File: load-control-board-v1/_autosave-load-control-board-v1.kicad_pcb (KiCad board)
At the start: 4 copper layers, 100 x 80 mm, 94 parts, among them CN1 3511232BMRS0BNA2, CN2 BTC22M4NBB4SCM, CN3 BTC22M4NBB4SCM, Q1 AO3400A, Q2 AO3400A, Q3 IRFP7530PBF, U1 LM317_SOT-223, U10 OPA188xxDBV, U11 OPA188xxDBV, U12 INA186A1IDCKR, U2 74AHC1G04, U22 TL081HIDBVR, U3 LM317_SOT-223, U5 REF5025AD, U6 SN74LVC1G123DCUR_C352969, U7 ALERT_COMP_OUT, U8 OPA188xxDBV

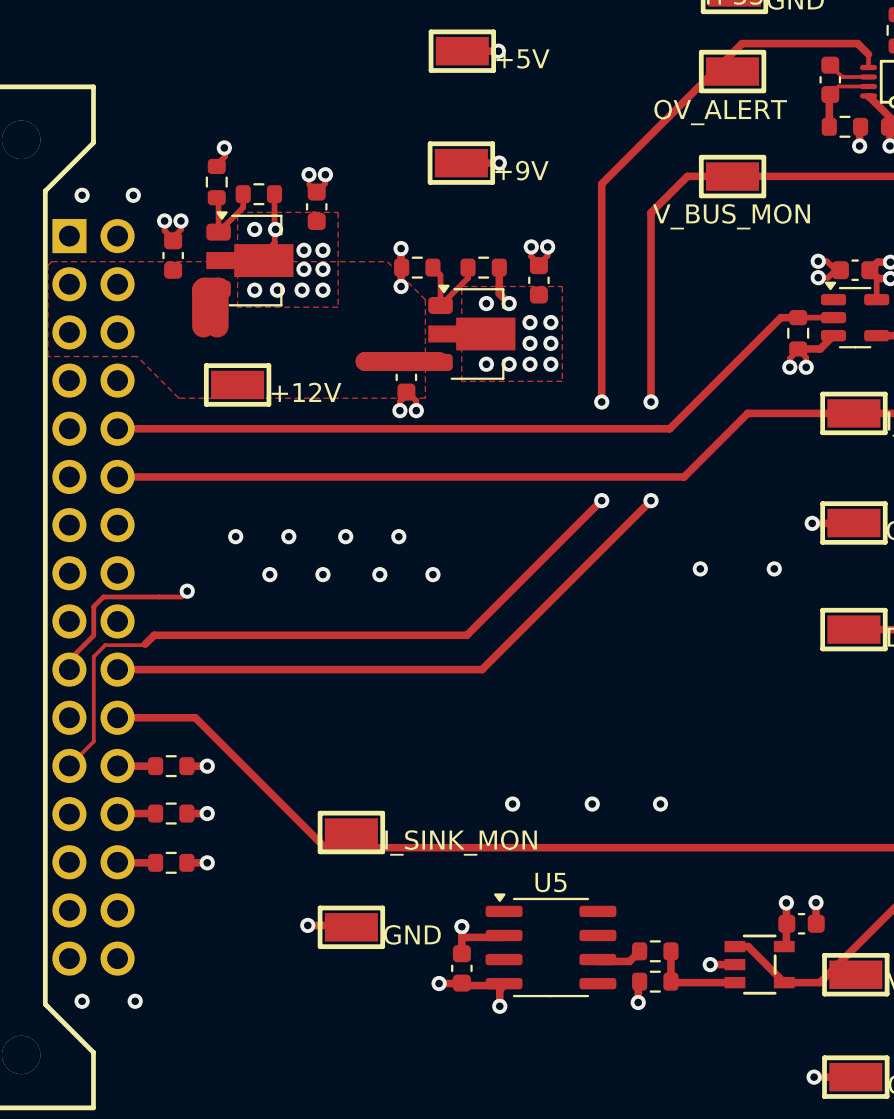
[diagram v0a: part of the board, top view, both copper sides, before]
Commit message: First complete PCB, DRC check complete
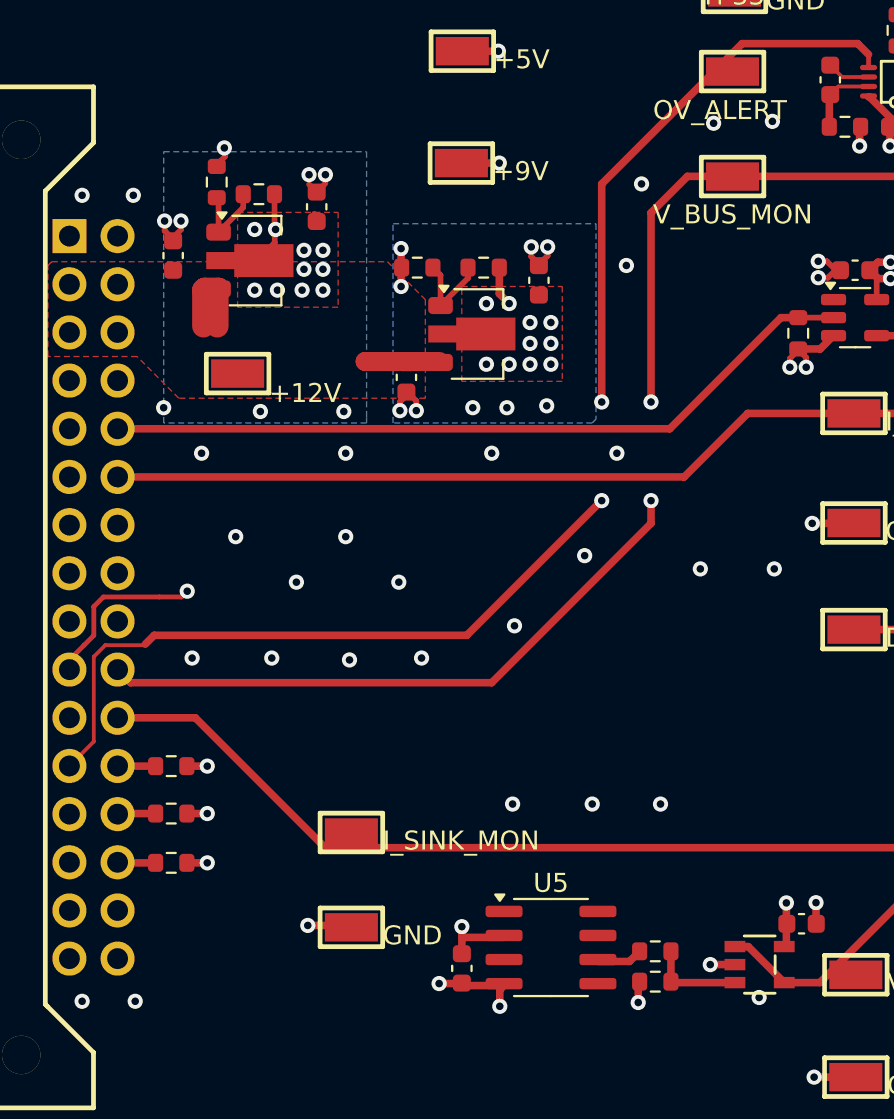
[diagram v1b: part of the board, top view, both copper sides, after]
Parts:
- moved TP1 0.60 mm to (75.6, 82.0)
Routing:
- net Net-(C18-Pad1): track 10.5 -> 13.9 mm
- net +9V: track 70.0 -> 73.2 mm
- net V_BUS_MON: track 71.8 -> 73.1 mm
- net GND: vias 101 -> 118
- added copper zone on B.Cu, net +5V
- added copper zone on B.Cu, net +9V
